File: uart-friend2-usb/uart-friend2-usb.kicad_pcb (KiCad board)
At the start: 2 copper layers, 40 parts, among them J1 USB_C_Receptacle_USB2.0, P1 USB_A_Plug_PCB, P2 USB_C_Plug_USB2.0_16P, P3 USB_C_Plug_USB2.0_16P, P4 USB_C_Plug_USB3.0_9P, U1 RP2040, U2 W25Q128JVPIQ, U3 NCP1117-3.3_SOT223, Y1 12MHz

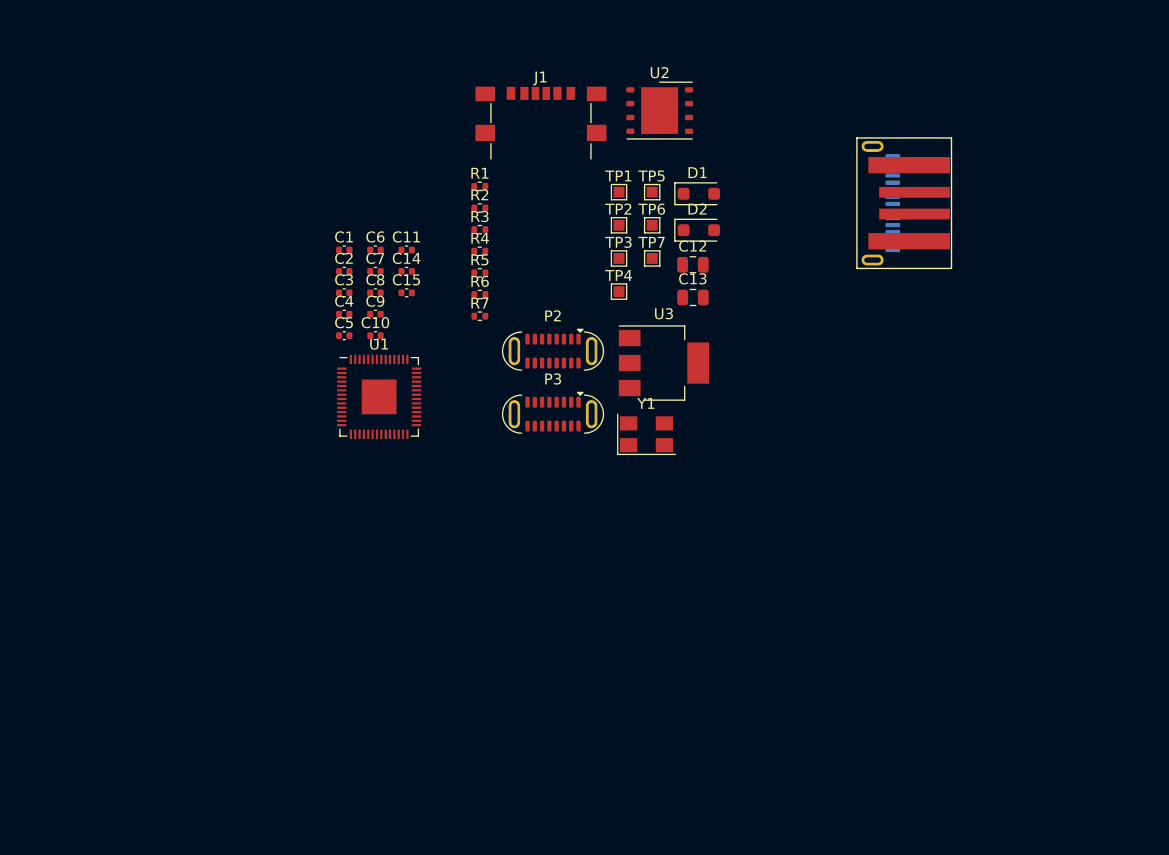
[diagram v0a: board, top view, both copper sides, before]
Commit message: resolve uart-friend2-usb footprint issues
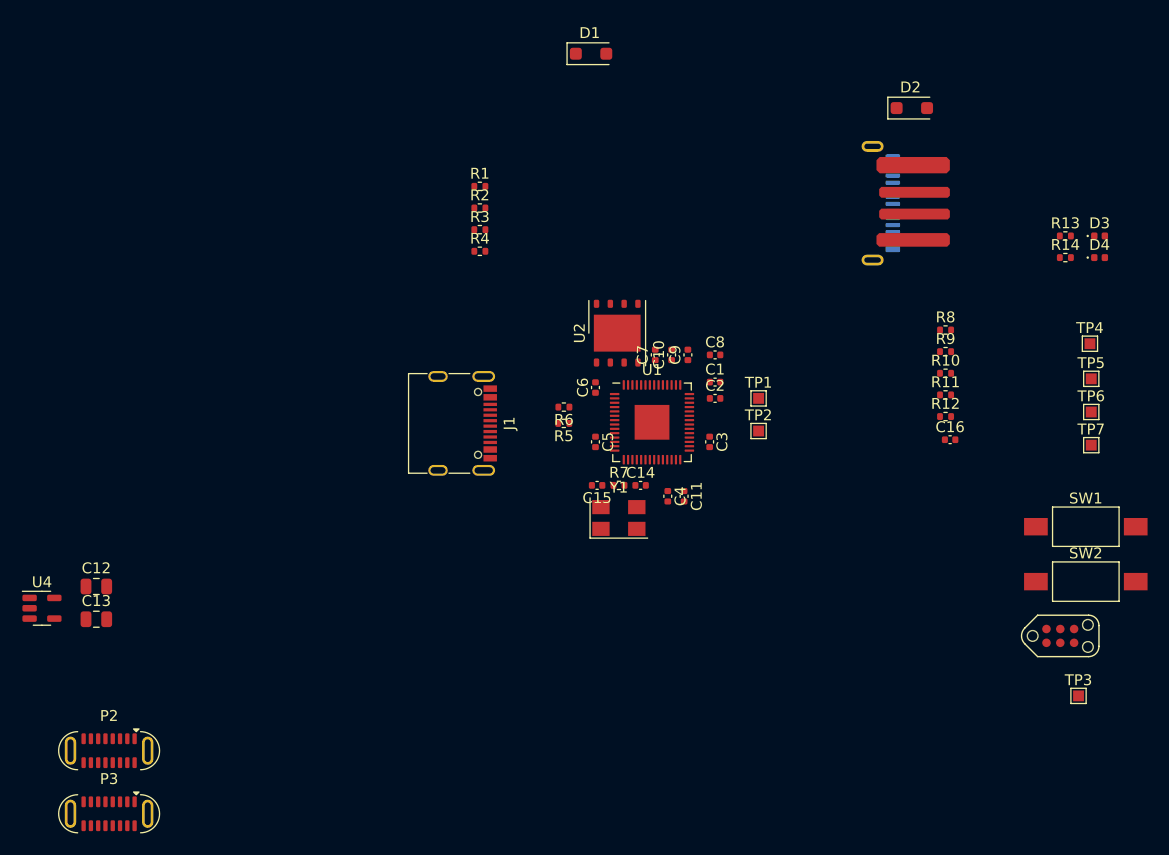
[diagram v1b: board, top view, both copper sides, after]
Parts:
- removed U3: NCP1117-3.3_SOT223, Package_TO_SOT_SMD:SOT-223-3_TabPin2
- added C16: 0.1uF, Capacitor_SMD:C_0402_1005Metric, F.Cu at (174.0, 108.5)
- added D3: Green, LED_SMD:LED_0402_1005Metric, F.Cu at (187.8, 89.8)
- added D4: Green, LED_SMD:LED_0402_1005Metric, F.Cu at (187.8, 91.8)
- added J2: Conn_02x03_Odd_Even, uart-friend2-usb-special:TC2030-NL_SMALL, F.Cu at (184.2, 126.5)
- added R10: 5.1k, Resistor_SMD:R_0402_1005Metric, F.Cu at (173.6, 102.4)
- added R11: 5.1k, Resistor_SMD:R_0402_1005Metric, F.Cu at (173.6, 104.4)
- added R12: 5.1k, Resistor_SMD:R_0402_1005Metric, F.Cu at (173.6, 106.4)
- added R13: 5.1k, Resistor_SMD:R_0402_1005Metric, F.Cu at (184.6, 89.8)
- added R14: 5.1k, Resistor_SMD:R_0402_1005Metric, F.Cu at (184.6, 91.8)
- added R8: 1k, Resistor_SMD:R_0402_1005Metric, F.Cu at (173.6, 98.4)
- added R9: 5.1k, Resistor_SMD:R_0402_1005Metric, F.Cu at (173.6, 100.4)
- added SW1: BOOT, Button_Switch_SMD:SW_SPST_FSMSM, F.Cu at (186.5, 116.5)
- added SW2: RST, Button_Switch_SMD:SW_SPST_FSMSM, F.Cu at (186.5, 121.5)
- added U4: AP7366-33W5-7, Package_TO_SOT_SMD:SOT-23-5, F.Cu at (90.5, 124.0)
- J1: footprint Connector_USB:USB_C_Receptacle_GCT_USB4135-GF-A_6P_TopMnt_Horizontal -> Connector_USB:USB_C_Receptacle_G-Switch_GT-USB-7010ASV
- P1: footprint uart-friend2-usb-special:USB_A_Plug_PCB_SparkFun -> uart-friend2-usb-special:USB_A_Plug_PCB_Shorter_Pads
- moved C12 62.3 mm to (95.5, 122.0)
- moved C13 62.3 mm to (95.5, 125.0)
- moved TP3 58.3 mm to (185.8, 132.1)
- moved P2 54.9 mm to (96.7, 137.1)
- moved P3 54.9 mm to (96.7, 142.9)
- moved TP5 43.9 mm to (187.0, 102.9)
- moved TP6 43.9 mm to (187.0, 106.0)
- moved TP7 43.9 mm to (187.0, 109.0)
- moved TP4 43.6 mm to (186.9, 99.7)
- moved C3 36.3 mm to (151.9, 108.7), turned to -90 degrees
- moved C1 36.2 mm to (152.4, 103.2)
- moved C2 36.0 mm to (152.4, 104.7)
- moved C4 34.1 mm to (148.1, 113.7), turned to -90 degrees
- moved C11 34.1 mm to (149.6, 113.7), turned to -90 degrees
- moved C8 31.8 mm to (152.4, 100.7)
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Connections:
- J1 pad A5: unconnected-(J1-CC1-PadA5) -> /J1_CC1
- J1 pad B5: unconnected-(J1-CC2-PadB5) -> /J2_CC2
- P2 pad A5: unconnected-(P2-CC-PadA5) -> Net-(P2-CC)
- P2 pad B6: /USB0_R_P -> unconnected-(P2-D+-PadB6)
- P2 pad B7: /USB0_R_N -> unconnected-(P2-D--PadB7)
- P3 pad A6: /USB1_P -> /USB1_R_P
- P3 pad A7: /USB1_N -> /USB1_R_N
- P3 pad B6: /USB1_P -> unconnected-(P3-D+-PadB6)
- P3 pad B7: /USB1_N -> unconnected-(P3-D--PadB7)
- P4 pad A5: unconnected-(P4-CC-PadA5) -> /P4_CC
- P4 pad A9: Net-(P4-VBUS-PadA4) -> /VBUS0
- R5 pad 1: Net-(U1-GPIO1) -> /USB1_N
- R5 pad 2: /USB1_N -> /USB1_R_N
- R6 pad 1: Net-(U1-GPIO0) -> /USB1_P
- R6 pad 2: /USB1_P -> /USB1_R_P
- TP1 pad 1: unconnected-(TP1-Pad1) -> /ADC1
- TP2 pad 1: /SWD_CLK -> /ADC2
- TP3 pad 1: /SWD -> /SWD_OUT
- U1 pad 11: unconnected-(U1-GPIO8-Pad11) -> /LED_GPIO8
- U1 pad 2: Net-(U1-GPIO0) -> /USB1_P
- U1 pad 3: Net-(U1-GPIO1) -> /USB1_N
- U1 pad 39: unconnected-(U1-GPIO27_ADC1-Pad39) -> /ADC1
- U1 pad 40: unconnected-(U1-GPIO28_ADC2-Pad40) -> /ADC2
- U1 pad 9: unconnected-(U1-GPIO7-Pad9) -> /LED_GPIO7

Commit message: uart-friend2-usb floorplan and some layout
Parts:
- removed C8: 0.1uF, Capacitor_SMD:C_0402_1005Metric
- added D5: Green, LED_SMD:LED_0402_1005Metric, F.Cu at (159.8, 104.8)
- added D6: Green, LED_SMD:LED_0402_1005Metric, F.Cu at (130.0, 113.8)
- added R15: 5.1k, Resistor_SMD:R_0402_1005Metric, F.Cu at (162.0, 104.8)
- added R16: 5.1k, Resistor_SMD:R_0402_1005Metric, F.Cu at (127.8, 113.8)
- added U3: WE-TVS-82400102, Package_TO_SOT_SMD:SOT-23-6, F.Cu at (160.8, 102.2)
- added U5: WE-TVS-82400102, Package_TO_SOT_SMD:SOT-23-6, F.Cu at (136.0, 107.5)
- C12, C13: value 4.7uF -> 2.2uF; footprint Capacitor_SMD:C_0805_2012Metric -> Capacitor_SMD:C_0603_1608Metric
- D3, D4: value Green -> Orange
- J2, P2, P3, TP1, TP2, TP3, TP4, TP5, TP6, TP7: moved to B.Cu
- moved U4 79.1 mm to (167.2, 105.0)
- moved C13 78.5 mm to (170.5, 102.0), turned to 90 degrees
- moved C12 76.8 mm to (170.5, 105.2), turned to -90 degrees
- moved P2 69.6 mm to (161.0, 110.5), turned to 90 degrees
- moved P3 51.3 mm to (133.8, 107.5), turned to 90 degrees
- moved D3 50.5 mm to (141.5, 110.0)
- moved D4 49.3 mm to (141.5, 108.8)
- moved R10 45.9 mm to (127.8, 101.2), turned to 180 degrees
- moved R13 45.6 mm to (143.8, 110.0), turned to 180 degrees
- moved R14 44.3 mm to (143.8, 108.8), turned to 180 degrees
- moved R9 43.6 mm to (130.0, 101.2)
- moved TP3 41.5 mm to (150.2, 110.8), turned to 180 degrees
- moved J2 35.5 mm to (151.2, 113.3), turned to 180 degrees
- moved R1 30.9 mm to (157.0, 101.5), turned to 180 degrees
- moved R2 30.5 mm to (157.0, 102.8), turned to 180 degrees
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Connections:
- J1 pad A6: /USB1_R_P -> /USB1_D_P
- J1 pad A7: /USB1_R_N -> /USB1_D_N
- J1 pad B6: /USB1_R_P -> /USB1_D_P
- J1 pad B7: /USB1_R_N -> /USB1_D_N
- P2 pad A6: /USB0_R_P -> /USB0_D_P
- P2 pad A7: /USB0_R_N -> /USB0_D_N
- P3 pad A6: /USB1_R_P -> /USB1_D_P
- P3 pad A7: /USB1_R_N -> /USB1_D_N
- P4 pad A6: /USB0_R_P -> /USB0_D_P
- P4 pad A7: /USB0_R_N -> /USB0_D_N
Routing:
- net GND: track 0.00 -> 53.3 mm, vias 0 -> 21
- net /USB0_D_P: track 0.00 -> 38.1 mm, vias 0 -> 3
- net /USB0_D_N: track 0.00 -> 34.7 mm, vias 0 -> 3
- net /VBUS1: track 0.00 -> 21.5 mm, vias 0 -> 1
- net +3V3: track 0.00 -> 20.2 mm
- net Net-(U1-QSPI_SD2): track 0.00 -> 15.5 mm, vias 0 -> 2
- net /U1_XIN: track 0.00 -> 14.9 mm
- net /U1_EEPROM_SS_L: track 0.00 -> 14.5 mm, vias 0 -> 2
- net /U1_EEPROM_SD1: track 0.00 -> 13.6 mm, vias 0 -> 2
- net /USB1_D_N: track 0.00 -> 12.4 mm, vias 0 -> 2
- net /USB1_D_P: track 0.00 -> 11.0 mm, vias 0 -> 3
- net /J2_CC2: track 0.00 -> 10.9 mm
- net /U1_RUN: track 0.00 -> 9.31 mm
- net /USB1_R_P: track 0.00 -> 9.27 mm
- net /USB1_R_N: track 0.00 -> 9.27 mm
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- added copper zone on In1.Cu, net GND
- added copper zone on In2.Cu, net GND
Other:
- board outline added: 56.5 x 15.5 mm
- copper layers 2 -> 4

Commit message: uart-friend2-usb R1 layout schematic metadata production files
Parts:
- removed R11: 5.1k, Resistor_SMD:R_0402_1005Metric
- added REF**: MountingHole_1.152mm_JLCPCB_Tooling, uart-friend2-usb-special:MountingHole_1.152mm_JLCPCB_Tooling, F.Cu at (171.0, 114.5)
- added REF**: MountingHole_1.152mm_JLCPCB_Tooling, uart-friend2-usb-special:MountingHole_1.152mm_JLCPCB_Tooling, F.Cu at (126.0, 101.0)
- C14, C15: value 16pF -> 15pF
- D3, D4: value Orange -> Yellow; footprint LED_SMD:LED_0402_1005Metric -> LED_SMD:LED_0603_1608Metric
- D5, D6: footprint LED_SMD:LED_0402_1005Metric -> LED_SMD:LED_0603_1608Metric
- P2, P3: footprint uart-friend2-usb-special:USB_C_Plug_YIYUAN_YTC-TC16S-128_16P_Vertical -> Connector_PinHeader_1.00mm:PinHeader_1x05_P1.00mm_Vertical
- R7: value 7.2k -> 6.8k
- moved D4 11.6 mm to (131.0, 113.8)
- moved R4 11.3 mm to (147.8, 101.5), turned to 90 degrees
- moved R13 8.55 mm to (135.5, 112.2)
- moved R14 8.55 mm to (135.5, 111.0)
- moved D3 8.16 mm to (134.2, 113.8)
- moved P2 5.25 mm to (166.2, 110.5)
- moved D6 3.50 mm to (126.5, 113.8), turned to 0 degrees
- moved P3 2.61 mm to (134.5, 105.0), turned to 180 degrees
- moved D1 1.60 mm to (136.8, 102.8), turned to -90 degrees
- moved R16 1.03 mm to (128.8, 114.0), turned to -90 degrees
- moved R12 1.00 mm to (169.2, 112.8)
- moved J1 0.75 mm to (128.8, 107.5)
- moved R10 0.75 mm to (128.5, 101.2)
- moved R9 0.75 mm to (130.8, 101.2)
- moved U5 0.75 mm to (136.8, 107.5)
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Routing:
- net GND: track 53.3 -> 115.1 mm, vias 21 -> 48
- net /VBUS0: track 7.95 -> 49.8 mm, vias 1 -> 2
- net +3V3: track 20.2 -> 50.1 mm, vias 0 -> 9
- net /U1_BOOT: track 0.00 -> 15.1 mm, vias 0 -> 2
- net VDD: track 5.02 -> 18.2 mm, vias 0 -> 3
- net /LED_GPIO8: track 3.29 -> 15.9 mm
- net VBUS: track 0.00 -> 12.0 mm, vias 0 -> 5
- net /P4_CC: track 0.00 -> 11.5 mm, vias 0 -> 1
- net /VBUS1: track 21.5 -> 30.5 mm, vias 1 -> 4
- net /USB0_D_N: track 34.7 -> 27.5 mm, vias 3 -> 1
- net /USB0_D_P: track 38.1 -> 30.9 mm, vias 3 -> 1
- net /LED_GPIO7: track 6.32 -> 13.3 mm
- net Net-(D4-A): track 0.00 -> 4.56 mm
- net /U1_XIN: track 14.9 -> 17.3 mm
- net Net-(D6-A): track 0.00 -> 1.78 mm
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- added copper zone on In2.Cu, net +3V3
- added copper zone on In2.Cu, net VBUS
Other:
- board size 56.5 x 15.5 mm -> 56.2 x 15.5 mm
- board text added: "CC"
- board text added: "RX"
- board text added: "RX1N"
- board text added: "Reset"
- board text added: "SWD Dbg"
- board text added: "TX"
- board text added: "TX1P"
- board text added: "USB Boot"
- board text added: "V0"
- board text added: "V1"
- board text added: "VG+-G"
- board text added: "ihartwig 2023 R1"
- board text added: "uart-friend2-usb"
